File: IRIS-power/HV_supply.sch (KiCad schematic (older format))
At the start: 17 parts, among them U41 TPS55340

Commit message: Improved fuel gauge layout
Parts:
- C41: Digikey PN (none) -> 1276-1192-1-ND
- C42: Digikey PN (none) -> 1276-CL10B104KB8NNNLCT-ND
- C43: Digikey PN (none) -> 1276-1814-1-ND
- C44: Digikey PN (none) -> 1276-1951-1-ND
- C45: Digikey PN (none) -> 1276-2025-1-ND
- C46: Digikey PN (none) -> 1276-3387-1-ND
- C47: Digikey PN (none) -> 587-3506-1-ND
- R44: Digikey PN (none) -> RNCP0603FTD10K0CT-ND
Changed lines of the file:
@@
 F 2 "Capacitor_SMD:C_0603_1608Metric" H 5438 4100 50  0001 C CNN
 F 3 "~" H 5400 4250 50  0001 C CNN
+F 4 "1276-2025-1-ND" H 5400 4250 50  0001 C CNN "Digikey PN"
 	1    5400 4250
 	1    0    0    -1
@@
 F 3 "~" H 3450 3750 50  0001 C CNN
 F 4 "X5R, 16V" H 3450 3750 50  0001 C CNN "Notes"
+F 5 "1276-1192-1-ND" H 3450 3750 50  0001 C CNN "Digikey PN"
 	1    3450 3750
 	1    0    0    -1
@@
 F 2 "Resistor_SMD:R_0603_1608Metric" V 6830 4050 50  0001 C CNN
 F 3 "~" H 6900 4050 50  0001 C CNN
+F 4 "RNCP0603FTD10K0CT-ND" H 6900 4050 50  0001 C CNN "Digikey PN"
 	1    6900 4050
 	1    0    0    -1
@@
 F 2 "Capacitor_SMD:C_0805_2012Metric" H 7638 3250 50  0001 C CNN
 F 3 "1276-3387-1-ND" H 7600 3400 50  0001 C CNN
+F 4 "1276-3387-1-ND" H 7600 3400 50  0001 C CNN "Digikey PN"
 	1    7600 3400
 	1    0    0    -1
@@
 F 2 "Capacitor_SMD:C_0603_1608Metric" H 4138 4100 50  0001 C CNN
 F 3 "~" H 4100 4250 50  0001 C CNN
+F 4 "1276-1814-1-ND" H 4100 4250 50  0001 C CNN "Digikey PN"
 	1    4100 4250
 	1    0    0    -1
@@
 F 2 "Capacitor_SMD:C_0603_1608Metric" H 4638 4100 50  0001 C CNN
 F 3 "~" H 4600 4250 50  0001 C CNN
+F 4 "1276-1951-1-ND" H 4600 4250 50  0001 C CNN "Digikey PN"
 	1    4600 4250
 	1    0    0    -1
@@
 F 2 "Capacitor_SMD:C_0603_1608Metric" H 3888 3600 50  0001 C CNN
 F 3 "~" H 3850 3750 50  0001 C CNN
+F 4 "1276-CL10B104KB8NNNLCT-ND" H 3850 3750 50  0001 C CNN "Digikey PN"
 	1    3850 3750
 	1    0    0    -1
@@
 F 2 "Capacitor_SMD:C_0603_1608Metric" H 8038 3250 50  0001 C CNN
 F 3 "~" H 8000 3400 50  0001 C CNN
+F 4 "587-3506-1-ND" H 8000 3400 50  0001 C CNN "Digikey PN"
 	1    8000 3400
 	1    0    0    -1

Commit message: Adjusted silkscreen
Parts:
- D41: footprint Diode_SMD:D_SMA_Handsoldering -> Diode_SMD:D_SMA
- R41: Digikey PN (none) -> RNCP0603FTD2K49CT-ND
- R42: Digikey PN (none) -> RMCF0603FT38K3CT-ND
- R43: Digikey PN (none) -> P232KHCT-ND
- U41: Digikey PN (none) -> 296-35493-5-ND
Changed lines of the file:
@@
 F 2 "Resistor_SMD:R_0603_1608Metric" V 4930 4250 50  0001 C CNN
 F 3 "~" H 5000 4250 50  0001 C CNN
+F 4 "RMCF0603FT38K3CT-ND" H 5000 4250 50  0001 C CNN "Digikey PN"
 	1    5000 4250
 	-1   0    0    1
@@
 F 2 "Resistor_SMD:R_0603_1608Metric" V 6830 3750 50  0001 C CNN
 F 3 "~" H 6900 3750 50  0001 C CNN
+F 4 "P232KHCT-ND" H 6900 3750 50  0001 C CNN "Digikey PN"
 	1    6900 3750
 	1    0    0    -1
@@
 F 2 "star-common-lib:TPS55340" H 6100 3700 50  0001 L CNN
 F 3 "" H 5850 3600 50  0001 C CNN
+F 4 "296-35493-5-ND" H 6100 3950 50  0001 C CNN "Digikey PN"
 	1    6100 3950
 	1    0    0    -1
@@
 F 0 "D41" H 6900 3125 50  0000 C CNN
 F 1 "D_Schottky" H 6900 3124 50  0001 C CNN
-F 2 "Diode_SMD:D_SMA_Handsoldering" H 6900 3250 50  0001 C CNN
+F 2 "Diode_SMD:D_SMA" H 6900 3250 50  0001 C CNN
 F 3 "https://www.comchiptech.com/admin/files/product/CDBA240LL-HF%20RevD765674.pdf" H 6900 3250 50  0001 C CNN
 F 4 "641-1698-1-ND" H 6900 3250 50  0001 C CNN "Digikey PN"
@@
 F 2 "Resistor_SMD:R_0603_1608Metric" V 4280 3900 50  0001 C CNN
 F 3 "~" H 4350 3900 50  0001 C CNN
+F 4 "RNCP0603FTD2K49CT-ND" H 4350 3900 50  0001 C CNN "Digikey PN"
 	1    4350 3900
 	0    1    1    0

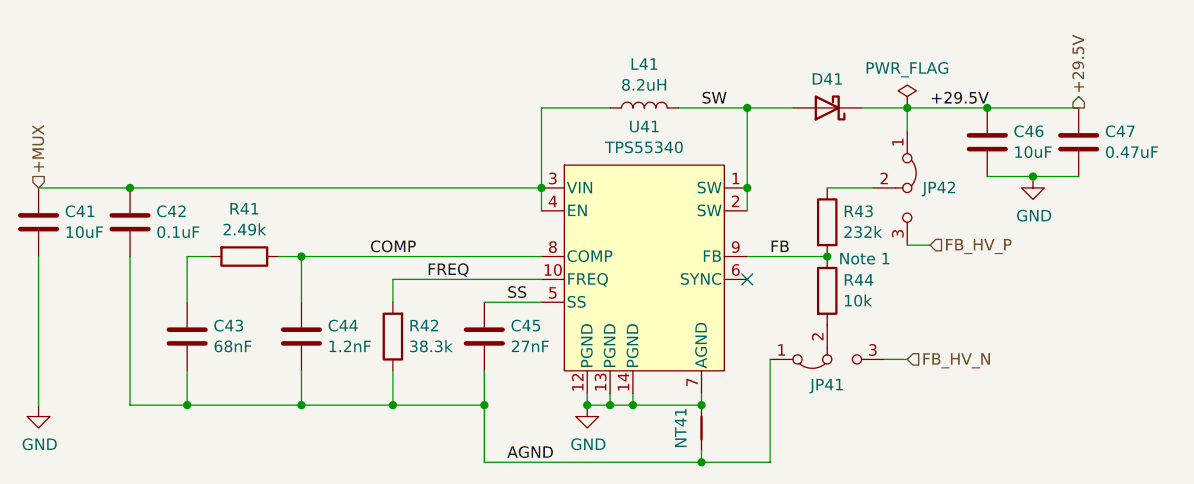
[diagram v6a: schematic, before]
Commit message: Updated HV supply
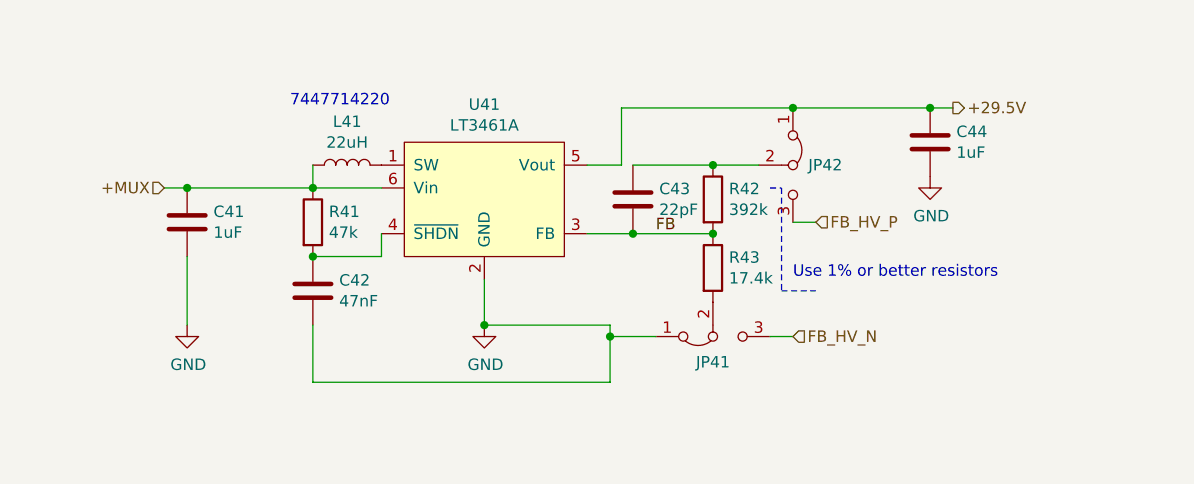
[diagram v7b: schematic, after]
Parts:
- removed C45: 27nF, Capacitor_SMD:C_0603_1608Metric, symbol Device:C
- removed C46: 10uF, Capacitor_SMD:C_0805_2012Metric, symbol Device:C
- removed C47: 0.47uF, Capacitor_SMD:C_0603_1608Metric, symbol Device:C
- removed D41: D_Schottky, Diode_SMD:D_SMA, symbol Device:D_Schottky
- removed NT41: Net-Tie_2, NetTie:NetTie-2_SMD_Pad0.5mm, symbol Device:Net-Tie_2
- removed R42: 38.3k, Resistor_SMD:R_0603_1608Metric, symbol Device:R
- removed U41: TPS55340, star-common-lib:TPS55340, symbol star-common-lib:TPS55340
- added U41: LT3461A, Package_TO_SOT_SMD:TSOT-23-6, symbol star-common-lib:LT3461A
- C41: value 10uF -> 1uF; Digikey PN 1276-1192-1-ND -> (none); Notes X5R, 16V -> (none)
- C42: value 0.1uF -> 47nF; Digikey PN 1276-CL10B104KB8NNNLCT-ND -> (none)
- C43: value 68nF -> 22pF; Digikey PN 1276-1814-1-ND -> (none)
- C44: value 1.2nF -> 1uF; Digikey PN 1276-1951-1-ND -> (none)
- L41: value 8.2uH -> 22uH; footprint star-common-lib:VLS6045AF -> star-common-lib:7447714220; Digikey PN 445-VLS6045AF-8R2MCT-ND -> (none); MFG PN VLS6045AF-8R2M -> (none); Unit Cost 0.54 -> (none)
- R41: value 2.49k -> 47k; Digikey PN RNCP0603FTD2K49CT-ND -> (none)
- R42: renamed from R43; value 232k -> 392k; footprint Resistor_SMD:R_0603_1608Metric -> Resistor_SMD:R_0805_2012Metric
- R43: renamed from R44; value 10k -> 17.4k; footprint Resistor_SMD:R_0603_1608Metric -> Resistor_SMD:R_0805_2012Metric
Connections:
- net +29.5V: now also C44.1, U41.5 (Vout)
- net +MUX: now also R41.1, U41.6 (Vin); no longer C42.1
- net FB: now also C43.2, U41.3 (FB)
- net GND: now also C42.2, C44.2, JP41.1 (A), U41.2 (GND)
- net at JP42.2 (C), R42.1: now also C43.1
- net at R41.2: now also C42.1, U41.4 (~SHDN); no longer C43.1
- removed net AGND: C42.2, C43.2, C44.2, JP41.1 (A)
- removed net COMP: C44.1, R41.1
- net SW: no longer names the net of L41.2
- net SW: now also U41.1 (SW)
- no-connect marks 1 -> 0
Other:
- note added: "7447714220"
- note added: "Use 1% or better resistors"
- note removed: "Note 1"
- moved on the sheet: JP41, JP42, R42, R43

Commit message: Updated to V4.01
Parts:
- C41, C44: Digikey PN (none) -> 1276-1860-1-ND
- C42: Digikey PN (none) -> 1276-2070-1-ND
- C43: Digikey PN (none) -> 1276-2228-1-ND
- L41: Digikey PN (none) -> 732-2992-1-ND
- R41: Digikey PN (none) -> P47.0KHCT-ND
- R42: Digikey PN P232KHCT-ND -> P21314CT-ND
- R43: Digikey PN RNCP0603FTD10K0CT-ND -> P21158CT-ND
- U41: Digikey PN (none) -> LT3461AES6#TRPBFCT-ND
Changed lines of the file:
@@
 F 2 "Resistor_SMD:R_0805_2012Metric" V 6330 3650 50  0001 C CNN
 F 3 "~" H 6400 3650 50  0001 C CNN
-F 4 "P232KHCT-ND" H 6400 3650 50  0001 C CNN "Digikey PN"
+F 4 "P21314CT-ND" H 6400 3650 50  0001 C CNN "Digikey PN"
 	1    6400 3650
 	1    0    0    -1
@@
 F 2 "Resistor_SMD:R_0805_2012Metric" V 6330 3950 50  0001 C CNN
 F 3 "~" H 6400 3950 50  0001 C CNN
-F 4 "RNCP0603FTD10K0CT-ND" H 6400 3950 50  0001 C CNN "Digikey PN"
+F 4 "P21158CT-ND" H 6400 3950 50  0001 C CNN "Digikey PN"
 	1    6400 3950
 	1    0    0    -1
@@
 F 2 "Capacitor_SMD:C_0603_1608Metric" H 4688 3900 50  0001 C CNN
 F 3 "~" H 4650 4050 50  0001 C CNN
+F 4 "1276-2070-1-ND" H 4650 4050 50  0001 C CNN "Digikey PN"
 	1    4650 4050
 	1    0    0    -1
@@
 F 2 "Resistor_SMD:R_0603_1608Metric" V 4580 3750 50  0001 C CNN
 F 3 "~" H 4650 3750 50  0001 C CNN
+F 4 "P47.0KHCT-ND" H 4650 3750 50  0001 C CNN "Digikey PN"
 	1    4650 3750
 	1    0    0    -1
@@
 F 2 "Capacitor_SMD:C_0603_1608Metric" H 4138 3600 50  0001 C CNN
 F 3 "~" H 4100 3750 50  0001 C CNN
+F 4 "1276-1860-1-ND" H 4100 3750 50  0001 C CNN "Digikey PN"
 	1    4100 3750
 	1    0    0    -1
@@
 F 2 "star-common-lib:7447714220" H 4800 3500 50  0001 C CNN
 F 3 "~" H 4800 3500 50  0001 C CNN
+F 4 "732-2992-1-ND" H 4800 3500 50  0001 C CNN "Digikey PN"
 	1    4800 3500
 	0    -1   -1   0
@@
 F 2 "Capacitor_SMD:C_0603_1608Metric" H 6088 3500 50  0001 C CNN
 F 3 "~" H 6050 3650 50  0001 C CNN
+F 4 "1276-2228-1-ND" H 6050 3650 50  0001 C CNN "Digikey PN"
 	1    6050 3650
 	1    0    0    -1
@@
 F 2 "Capacitor_SMD:C_0603_1608Metric" H 7388 3250 50  0001 C CNN
 F 3 "~" H 7350 3400 50  0001 C CNN
+F 4 "1276-1860-1-ND" H 7350 3400 50  0001 C CNN "Digikey PN"
 	1    7350 3400
 	1    0    0    -1
@@
 F 2 "Package_TO_SOT_SMD:TSOT-23-6" H 5400 3650 50  0001 C CNN
 F 3 "https://www.analog.com/media/en/technical-documentation/data-sheets/3461Afa.pdf" H 5400 3650 50  0001 C CNN
+F 4 "LT3461AES6#TRPBFCT-ND" H 5400 3650 50  0001 C CNN "Digikey PN"
 	1    5400 3650
 	1    0    0    -1
